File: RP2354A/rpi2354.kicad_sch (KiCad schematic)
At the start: 37 parts, among them J201 TC2030-NL, SW201 SW_Push_DPDT, U201 RP2354A, U202 NCP1117-3.3_SOT223, Y201 ABM8-272-T3

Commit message: Update RP2354 board with proper inductor symbol
.. and fix up the LED simulation a bit too.  I simulate LEDs with the
built-in diode model, but with N ("emission coefficient") set to 3,
which gets me a forward voltage around 2V.

But I think I should change RS ("series resistance") instead (or in
addition to).  See

    https://led-ld.nichia.co.jp/api/data/spec/tech/SP-QR-C2-210932-2-E_The%20SPICE%20Model%20of%20LEDs.pdf

which talks much more about this.

I guess I don't care that much, I just wanted the current simulation for
the power LED to be in roughly the right ballpark.

The inductor change is the relatively important thing here.

Signed-off-by: Linus Torvalds <torvalds@linux-foundation.org>
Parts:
- L201: footprint RP2350_60QFN_minimal:L_pol_2016 -> Mylib:AOTA-B2016; symbol Device:L -> Mylib:AOTA-B201610S3R3-101-T
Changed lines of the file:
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@@
 	)
 	(symbol
-		(lib_id "Device:L")
+		(lib_id "Mylib:AOTA-B201610S3R3-101-T")
 		(at 59.69 67.31 0)
 		(unit 1)
@@
 		(fields_autoplaced yes)
 		(property "Reference" "L201"
-			(at 60.96 66.04 0)
+			(at 60.96 66.0399 0)
 			(effects
 				(font
@@
 		)
 		(property "Value" "3.3u"
-			(at 60.96 68.58 0)
+			(at 60.96 68.5799 0)
 			(effects
 				(font
@@
 			)
 		)
-		(property "Footprint" "RP2350_60QFN_minimal:L_pol_2016"
-			(at 59.69 67.31 0)
-			(effects
-				(font
-					(size 1.27 1.27)
-				)
-				(hide yes)
-			)
-		)
-		(property "Datasheet" "~"
-			(at 59.69 67.31 0)
-			(effects
-				(font
-					(size 1.27 1.27)
-				)
-				(hide yes)
-			)
-		)
-		(property "Description" ""
-			(at 59.69 67.31 0)
-			(effects
-				(font
-					(size 1.27 1.27)
-				)
+		(property "Footprint" "Mylib:AOTA-B2016"
+			(at 59.69 87.63 0)
+			(effects
+				(font
+					(size 1.27 1.27)
+				)
+				(hide yes)
+			)
+		)
+		(property "Datasheet" "https://abracon.com/datasheets/AOTA-B201610S3R3-101-T.pdf"
+			(at 59.69 85.09 0)
+			(effects
+				(font
+					(size 1.27 1.27)
+				)
+				(hide yes)
+			)
+		)
+		(property "Description" "Inductor"
+			(at 59.69 82.55 0)
+			(effects
+				(font
+					(size 1.27 1.27)
+				)
+				(hide yes)
 			)
 		)
@@
 			(at 123.19 180.34 0)
 			(effects
+				(font
+					(size 1.27 1.27)
+				)
+				(hide yes)
+			)
+		)
+		(property "Sim.Device" "D"
+			(at 123.19 180.34 0)
+			(effects
+				(font
+					(size 1.27 1.27)
+				)
+				(hide yes)
+			)
+		)
+		(property "Sim.Params" "n=3"
+			(at 123.19 180.34 0)
+			(effects

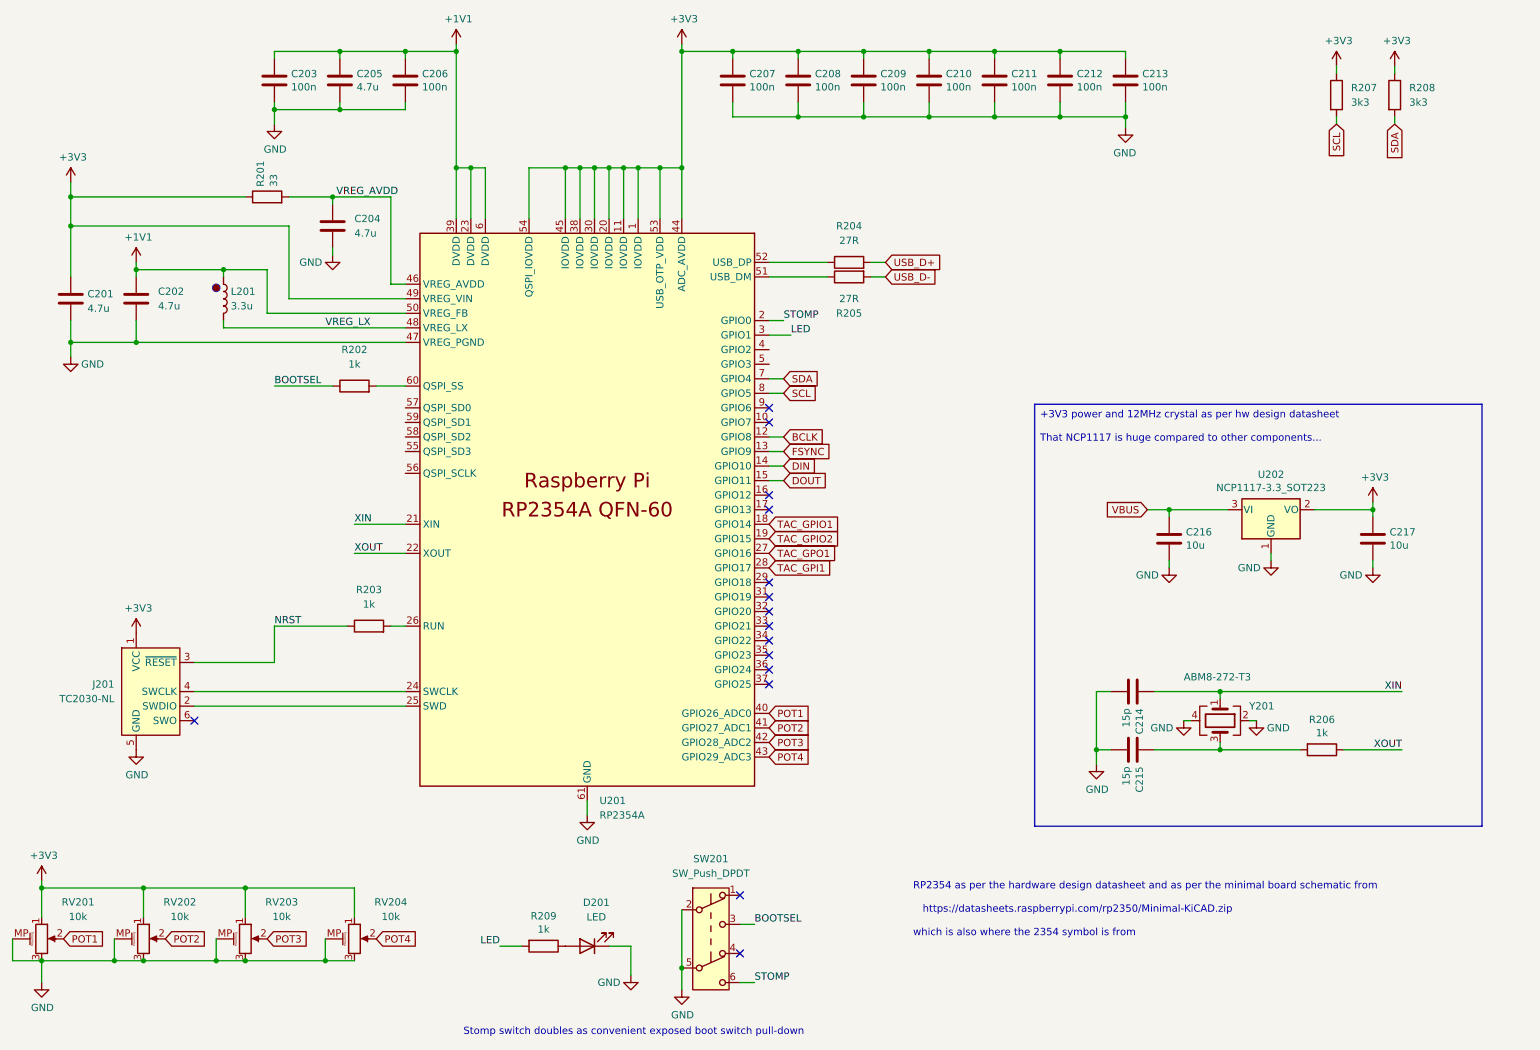
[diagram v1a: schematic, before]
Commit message: First cut at BOM selection for caps and resistors
The size choices were a bit random, this standardizes on 0402 for
resistors.  Also, optimize the BOM by just sharing values where they
don't matter that much.

For example, we need those 5k1 resistors for the USB CC pulldowns, and
we might as well then use that for the i2c pullup resistors too.  And
the self-biasing source resistor for the JFET input could use the same.

For similar reasons, just standardize on 33R for the low value resistors
that we use for the USB data line serial termination and the analog
voltage RC filtering.

Capacitors are 0402 for small values (0.1uF and smaller) or 0603 for
bigger capacitance values.  That seems to match availability.

Signed-off-by: Linus Torvalds <torvalds@linux-foundation.org>
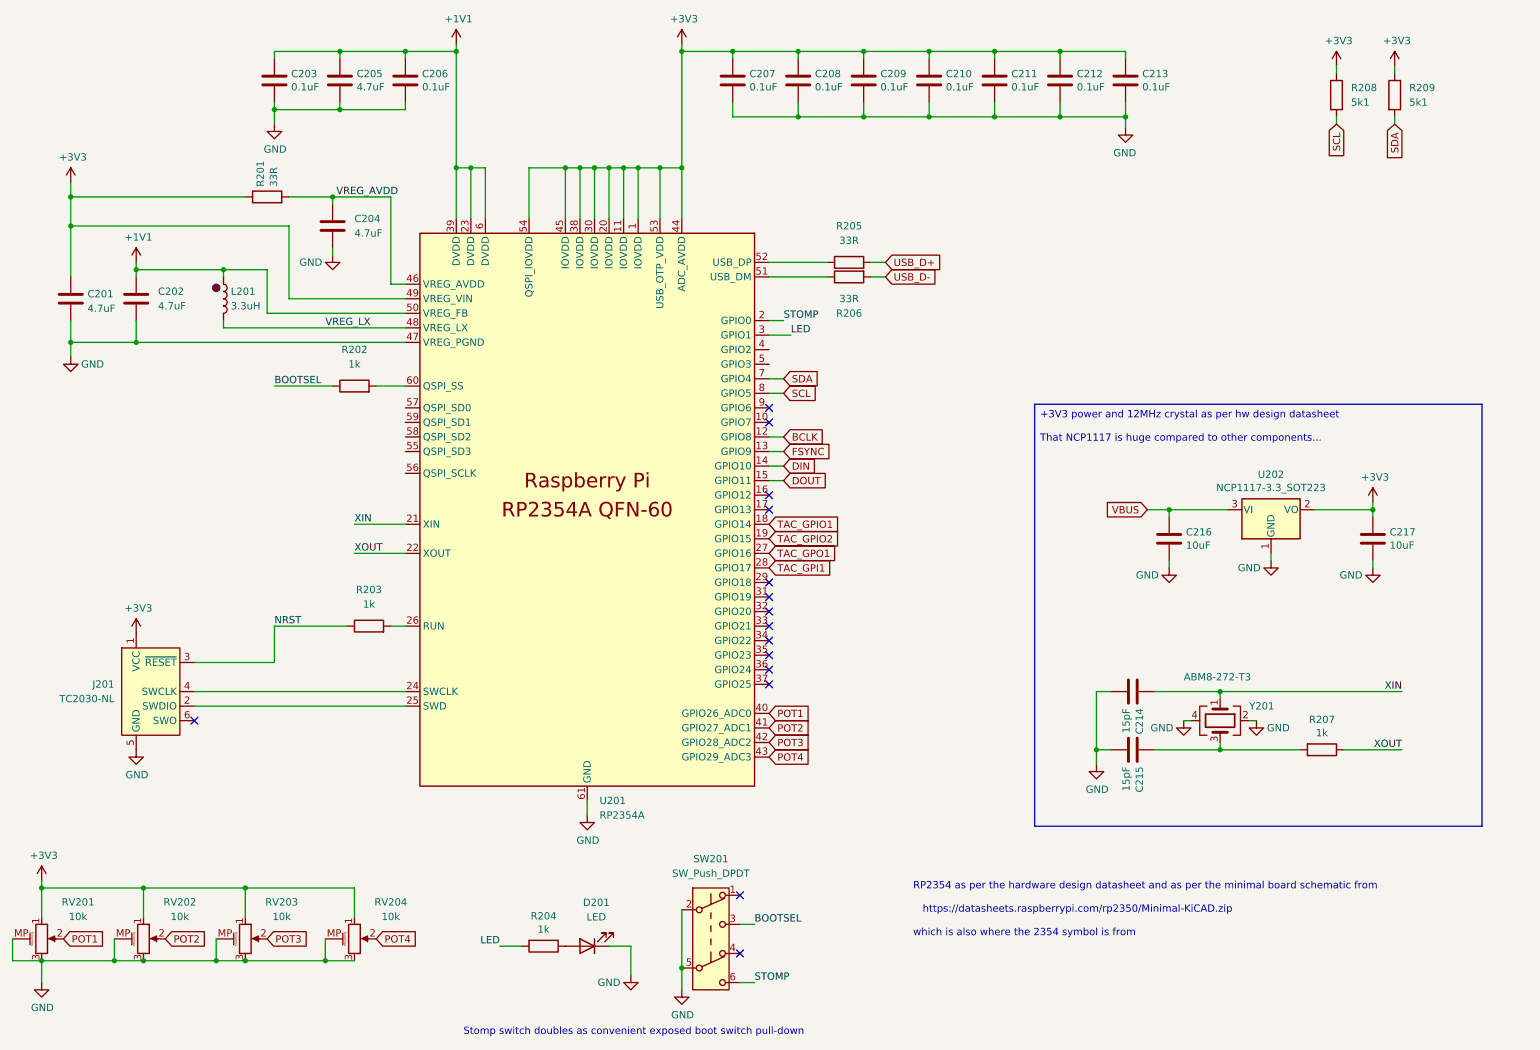
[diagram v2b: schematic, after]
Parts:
- C201, C202: value 4.7u -> 4.7uF; footprint Capacitor_SMD:C_0805_2012Metric -> Capacitor_SMD:C_0603_1608Metric
- C203, C206, C207, C208, C209, C210, C211, C212, C213: value 100n -> 0.1uF
- C204, C205: value 4.7u -> 4.7uF; footprint Capacitor_SMD:C_0402_1005Metric -> Capacitor_SMD:C_0603_1608Metric
- C214, C215: value 15p -> 15pF
- C216, C217: value 10u -> 10uF; footprint Capacitor_SMD:C_0805_2012Metric -> Capacitor_SMD:C_0603_1608Metric
- L201: value 3.3u -> 3.3uH
- R201: value 33 -> 33R
- R205: renamed from R204; value 27R -> 33R
- R206: renamed from R205; value 27R -> 33R
- R208: renamed from R207; value 3k3 -> 5k1
- R209: renamed from R208; value 3k3 -> 5k1; footprint Resistor_SMD:R_0603_1608Metric -> Resistor_SMD:R_0402_1005Metric
- renumbered R209 to R204, R206 to R207
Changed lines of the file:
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@@
 			)
 		)
-		(property "Value" "100n"
+		(property "Value" "0.1uF"
 			(at 151.511 30.353 0)
 			(effects
@@
 			)
 		)
-		(property "Value" "100n"
+		(property "Value" "0.1uF"
 			(at 162.941 30.353 0)
 			(effects
@@
 			)
 		)
-		(property "Value" "100n"
+		(property "Value" "0.1uF"
 			(at 174.371 30.353 0)
 			(effects
@@
 			)
 		)
-		(property "Value" "100n"
+		(property "Value" "0.1uF"
 			(at 185.801 30.353 0)
 			(effects
@@
 			)
 		)
-		(property "Value" "100n"
+		(property "Value" "0.1uF"
 			(at 197.231 30.353 0)
 			(effects
@@
 			)
 		)
-		(property "Value" "100n"
+		(property "Value" "0.1uF"
 			(at 208.661 30.353 0)
 			(effects
@@
 			)
 		)
-		(property "Value" "10u"
+		(property "Value" "10uF"
 			(at 227.711 110.363 0)
 			(effects
@@
 			)
 		)
-		(property "Footprint" "Capacitor_SMD:C_0805_2012Metric"
+		(property "Footprint" "Capacitor_SMD:C_0603_1608Metric"
 			(at 225.7552 113.03 0)
 			(effects
@@
 			)
 		)
-		(property "Value" "10u"
+		(property "Value" "10uF"
 			(at 263.271 110.363 0)
 			(effects
@@
 			)
 		)
-		(property "Footprint" "Capacitor_SMD:C_0805_2012Metric"
+		(property "Footprint" "Capacitor_SMD:C_0603_1608Metric"
 			(at 261.3152 113.03 0)
 			(effects
@@
 			)
 		)
-		(property "Value" "100n"
+		(property "Value" "0.1uF"
 			(at 94.361 30.353 0)
 			(effects
@@
 		(on_board yes)
 		(dnp no)
-		(property "Reference" "R207"
+		(property "Reference" "R208"
 			(at 256.54 30.4799 0)
 			(effects
@@
 			)
 		)
-		(property "Value" "3k3"
+		(property "Value" "5k1"
 			(at 256.54 33.02 0)
 			(effects
@@
 			(project "RP2354A"
 				(path "/9e337e0b-885b-4d2b-99a2-62cdd082c615/fee2f2f3-eeb9-41d6-a69c-8dc30c4ebf5f"
-					(reference "R207")
+					(reference "R208")
 					(unit 1)
 				)
@@
 			)
 		)
-		(property "Value" "100n"
+		(property "Value" "0.1uF"
 			(at 220.091 30.353 0)
 			(effects
@@
 		(on_board yes)
 		(dnp no)
-		(property "Reference" "R209"
+		(property "Reference" "R204"
 			(at 115.57 175.0822 90)
 			(effects
@@
 			(project "RP2354A"
 				(path "/9e337e0b-885b-4d2b-99a2-62cdd082c615/fee2f2f3-eeb9-41d6-a69c-8dc30c4ebf5f"
-					(reference "R209")
+					(reference "R204")
 					(unit 1)
 				)
@@
 		(dnp no)
 		(fields_autoplaced yes)
-		(property "Reference" "R204"
+		(property "Reference" "R205"
 			(at 168.91 54.61 90)
 			(effects
@@
 			)
 		)
-		(property "Value" "27R"
+		(property "Value" "33R"
 			(at 168.91 57.15 90)
 			(effects
@@
 			(project ""
 				(path "/9e337e0b-885b-4d2b-99a2-62cdd082c615/fee2f2f3-eeb9-41d6-a69c-8dc30c4ebf5f"
-					(reference "R204")
+					(reference "R205")
 					(unit 1)
 				)
@@
 			)
 		)
-		(property "Value" "33"
+		(property "Value" "33R"
 			(at 68.453 47.752 0)
 			(effects
@@
 			)
 		)
-		(property "Value" "4.7u"
+		(property "Value" "4.7uF"
 			(at 35.941 69.0122 0)
 			(effects
@@
 			)
 		)
-		(property "Footprint" "Capacitor_SMD:C_0805_2012Metric"
+		(property "Footprint" "Capacitor_SMD:C_0603_1608Metric"
 			(at 33.9852 71.12 0)
 			(effects
@@
 			)
 		)
-		(property "Value" "15p"
+		(property "Value" "15pF"
 			(at 217.297 148.971 0)
 			(effects
@@
 			)
 		)
-		(property "Value" "4.7u"
+		(property "Value" "4.7uF"
 			(at 48.26 68.58 0)
 			(effects
@@
 			)
 		)
-		(property "Footprint" "Capacitor_SMD:C_0805_2012Metric"
+		(property "Footprint" "Capacitor_SMD:C_0603_1608Metric"
 			(at 45.4152 71.12 0)
 			(effects
@@
 			)
 		)
-		(property "Value" "4.7u"
+		(property "Value" "4.7uF"
 			(at 82.55 55.88 0)
 			(effects
@@
 			)
 		)
-		(property "Footprint" "Capacitor_SMD:C_0402_1005Metric"
+		(property "Footprint" "Capacitor_SMD:C_0603_1608Metric"
 			(at 79.7052 58.42 0)
 			(effects
@@
 		(on_board yes)
 		(dnp no)
-		(property "Reference" "R206"
+		(property "Reference" "R207"
 			(at 251.46 140.7922 90)
 			(effects
@@
 			(project "RP2354A"
 				(path "/9e337e0b-885b-4d2b-99a2-62cdd082c615/fee2f2f3-eeb9-41d6-a69c-8dc30c4ebf5f"
-					(reference "R206")
+					(reference "R207")
 					(unit 1)
 				)
@@
 		(on_board yes)
 		(dnp no)
-		(property "Reference" "R205"
+		(property "Reference" "R206"
 			(at 168.91 69.85 90)
 			(effects
@@
 			)
 		)
-		(property "Value" "27R"
+		(property "Value" "33R"
 			(at 168.91 67.31 90)
 			(effects
@@
 			(project "RP2354A"
 				(path "/9e337e0b-885b-4d2b-99a2-62cdd082c615/fee2f2f3-eeb9-41d6-a69c-8dc30c4ebf5f"
-					(reference "R205")
+					(reference "R206")
 					(unit 1)
 				)
@@
 			)
 		)
-		(property "Value" "100n"
+		(property "Value" "0.1uF"
 			(at 71.501 30.353 0)
 			(effects
@@
 			)
 		)
-		(property "Value" "4.7u"
+		(property "Value" "4.7uF"
 			(at 82.931 30.353 0)
 			(effects
@@
 			)
 		)
-		(property "Footprint" "Capacitor_SMD:C_0402_1005Metric"
+		(property "Footprint" "Capacitor_SMD:C_0603_1608Metric"
 			(at 80.9752 33.02 0)
 			(effects
@@
 			)
 		)
-		(property "Value" "3.3u"
+		(property "Value" "3.3uH"
 			(at 60.96 68.5799 0)
 			(effects
@@
 			)
 		)
-		(property "Value" "15p"
+		(property "Value" "15pF"
 			(at 217.297 138.811 0)
 			(effects
@@
 		(on_board yes)
 		(dnp no)
-		(property "Reference" "R208"
+		(property "Reference" "R209"
 			(at 266.7 30.4799 0)
 			(effects
@@
 			)
 		)
-		(property "Value" "3k3"
+		(property "Value" "5k1"
 			(at 266.7 33.02 0)
 			(effects
@@
 			)
 		)
-		(property "Footprint" "Resistor_SMD:R_0603_1608Metric"
+		(property "Footprint" "Resistor_SMD:R_0402_1005Metric"
 			(at 262.382 31.75 90)
 			(effects
@@
 			(project "RP2354A"
 				(path "/9e337e0b-885b-4d2b-99a2-62cdd082c615/fee2f2f3-eeb9-41d6-a69c-8dc30c4ebf5f"
-					(reference "R208")
+					(reference "R209")
 					(unit 1)
 				)

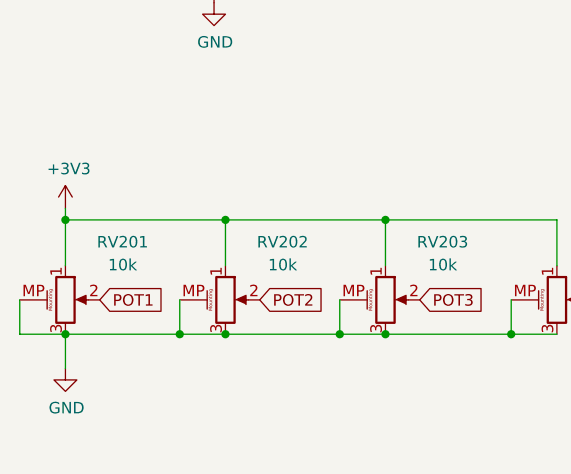
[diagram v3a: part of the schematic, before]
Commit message: Replace two of the pots with basic ones without mounting pins
... for the most ridiculous of reasons: it frees up some board space
without altering the physical layout of knobs.

I can't replace all the pots with the basic ones, because the pots
themselves are physically bigger and won't fit, but this odd mix of
potentiometer types works, even if it's all kinds of odd.

Does this board need to be this form factor? No.  I could just move
things around.  But I like the size, I like the bigger 20mm diameter
knobs I'm planning on using, and I'm just doing this ridiculous thing
for fun in the first place, so having a fun form factor is part of it
all.

The ridiculous reason for having four knobs in the first place? That's
how many ADCs the RP2354A has. So this is all very random.

Next up: do a 4-layer stackup and actually start laying things out.

Signed-off-by: Linus Torvalds <torvalds@linux-foundation.org>
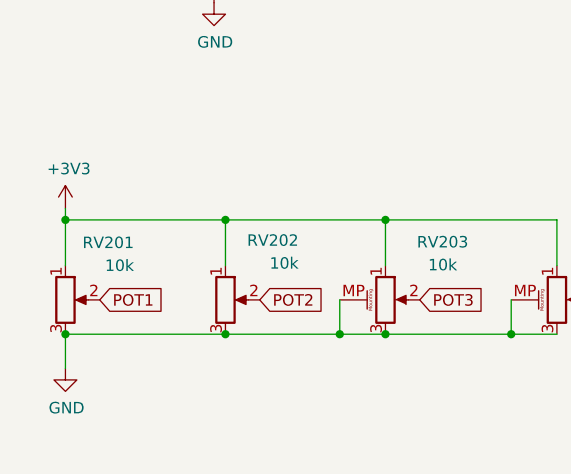
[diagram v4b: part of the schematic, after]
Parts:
- RV201, RV202: footprint Mylib:Potentiometer_9mm_MP -> Mylib:Potentiometer-Basic; symbol Device:R_Potentiometer_MountingPin -> Device:R_Potentiometer
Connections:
- net GND: no longer RV201.MP (MountPin), RV202.MP (MountPin)
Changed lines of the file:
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@@
 	)
 	(junction
-		(at 40.64 182.88)
-		(diameter 0)
-		(color 0 0 0 0)
-	)
-	(junction
 		(at 63.5 182.88)
 		(diameter 0)
@@
 	(wire
 		(pts
-			(xy 22.86 179.07) (xy 22.86 182.88)
-		)
-		(stroke
-			(width 0)
-			(type default)
-		)
-	)
-	(wire
-		(pts
-			(xy 40.64 179.07) (xy 40.64 182.88)
-		)
-		(stroke
-			(width 0)
-			(type default)
-		)
-	)
-	(wire
-		(pts
 			(xy 172.72 63.5) (xy 175.26 63.5)
 		)
@@
 	(wire
 		(pts
-			(xy 27.94 182.88) (xy 40.64 182.88)
-		)
-		(stroke
-			(width 0)
-			(type default)
-		)
-	)
-	(wire
-		(pts
 			(xy 154.94 83.82) (xy 157.48 83.82)
 		)
@@
 	(wire
 		(pts
-			(xy 40.64 182.88) (xy 45.72 182.88)
+			(xy 27.94 182.88) (xy 45.72 182.88)
 		)
 		(stroke
@@
 	(wire
 		(pts
-			(xy 22.86 182.88) (xy 27.94 182.88)
-		)
-		(stroke
-			(width 0)
-			(type default)
-		)
-	)
-	(wire
-		(pts
 			(xy 139.7 24.13) (xy 139.7 44.45)
 		)
@@
 	)
 	(symbol
-		(lib_id "Device:R_Potentiometer_MountingPin")
+		(lib_id "Device:R_Potentiometer")
 		(at 27.94 179.07 0)
 		(unit 1)
@@
 		(on_board yes)
 		(dnp no)
-		(fields_autoplaced yes)
 		(property "Reference" "RV201"
-			(at 34.29 172.6498 0)
+			(at 35.56 172.72 0)
 			(effects
 				(font
 					(size 1.27 1.27)
 				)
+				(justify right)
 			)
 		)
 		(property "Value" "10k"
-			(at 34.29 175.1898 0)
+			(at 35.56 175.26 0)
 			(effects
 				(font
 					(size 1.27 1.27)
 				)
+				(justify right)
 			)
 		)
-		(property "Footprint" "Mylib:Potentiometer_9mm_MP"
+		(property "Footprint" "Mylib:Potentiometer-Basic"
 			(at 27.94 179.07 0)
 			(effects
@@
 			)
 		)
-		(property "Description" "Potentiometer with a mounting pin"
+		(property "Description" "Potentiometer"
 			(at 27.94 179.07 0)
 			(effects
@@
 		(pin "2"
 		)
-		(pin "MP"
-		)
 		(pin "3"
 		)
@@
 	)
 	(symbol
-		(lib_id "Device:R_Potentiometer_MountingPin")
+		(lib_id "Device:R_Potentiometer")
 		(at 45.72 179.07 0)
 		(unit 1)
@@
 		(on_board yes)
 		(dnp no)
-		(fields_autoplaced yes)
 		(property "Reference" "RV202"
-			(at 52.07 172.6498 0)
+			(at 53.848 172.466 0)
 			(effects
 				(font
 					(size 1.27 1.27)
 				)
+				(justify right)
 			)
 		)
 		(property "Value" "10k"
-			(at 52.07 175.1898 0)
+			(at 53.848 175.006 0)
 			(effects
 				(font
 					(size 1.27 1.27)
 				)
+				(justify right)
 			)
 		)
-		(property "Footprint" "Mylib:Potentiometer_9mm_MP"
+		(property "Footprint" "Mylib:Potentiometer-Basic"
 			(at 45.72 179.07 0)
 			(effects
@@
 			)
 		)
-		(property "Description" "Potentiometer with a mounting pin"
+		(property "Description" "Potentiometer"
 			(at 45.72 179.07 0)
 			(effects
@@
 		(pin "2"
 		)
-		(pin "MP"
-		)
 		(pin "3"
